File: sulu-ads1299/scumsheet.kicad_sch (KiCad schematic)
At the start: 23 parts

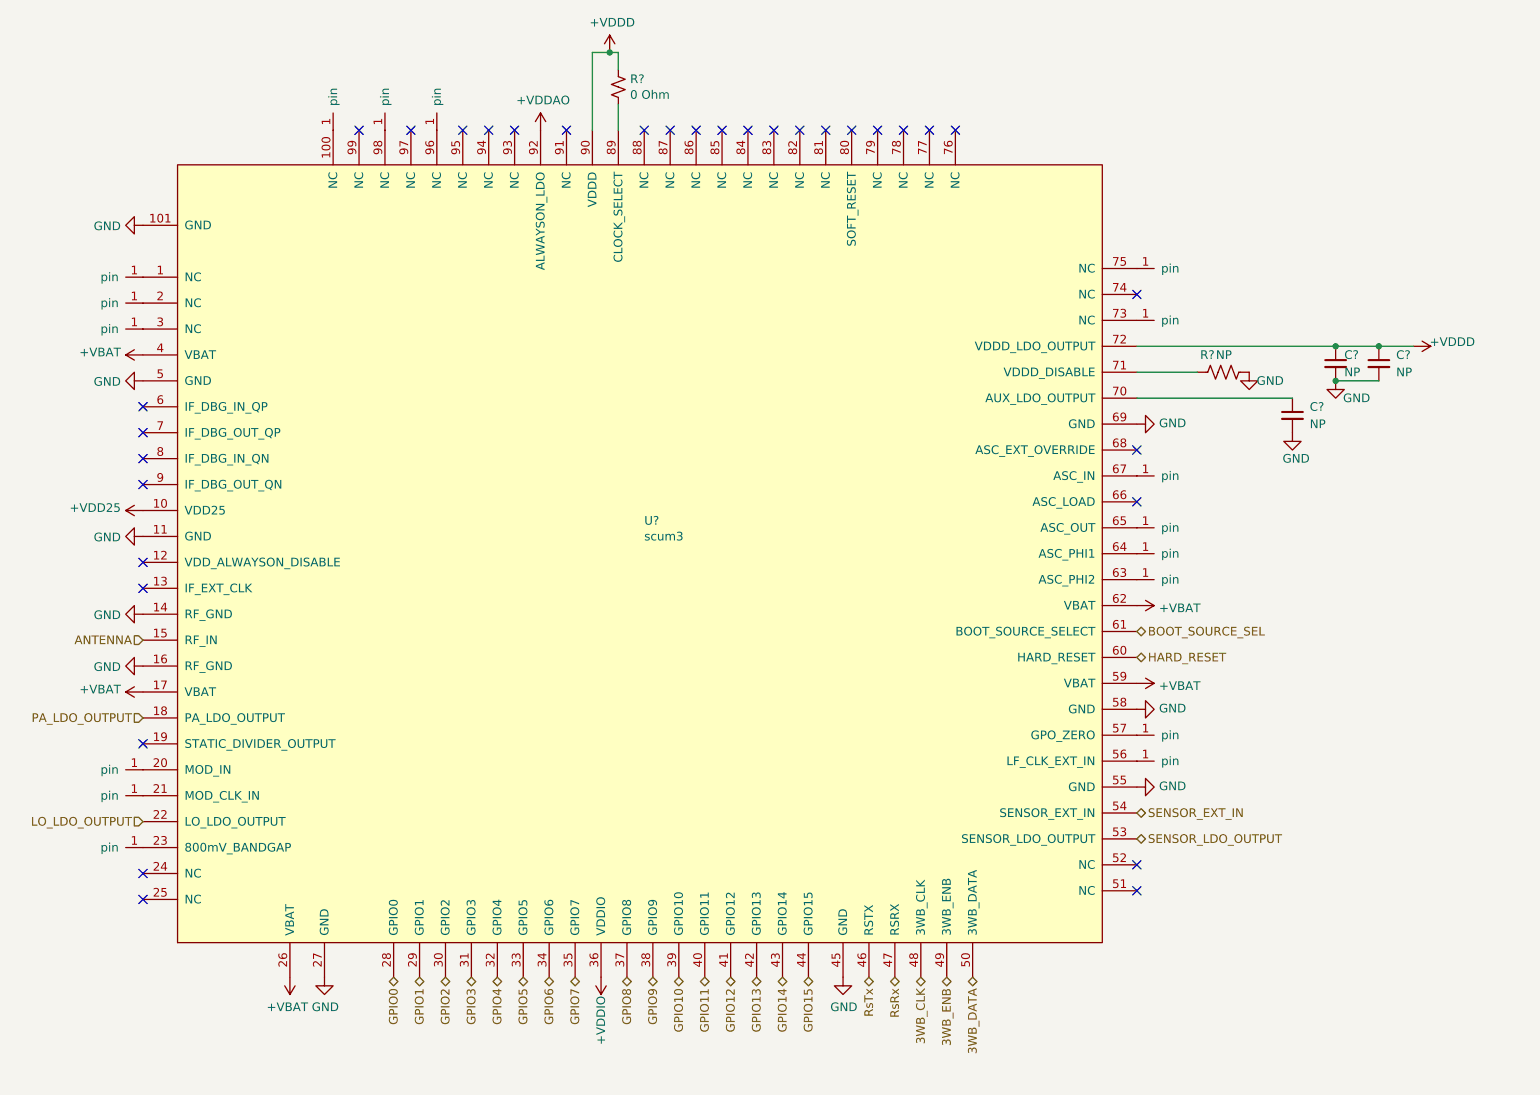
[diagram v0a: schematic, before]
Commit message: Sulu-ads1299 schematic largely completed
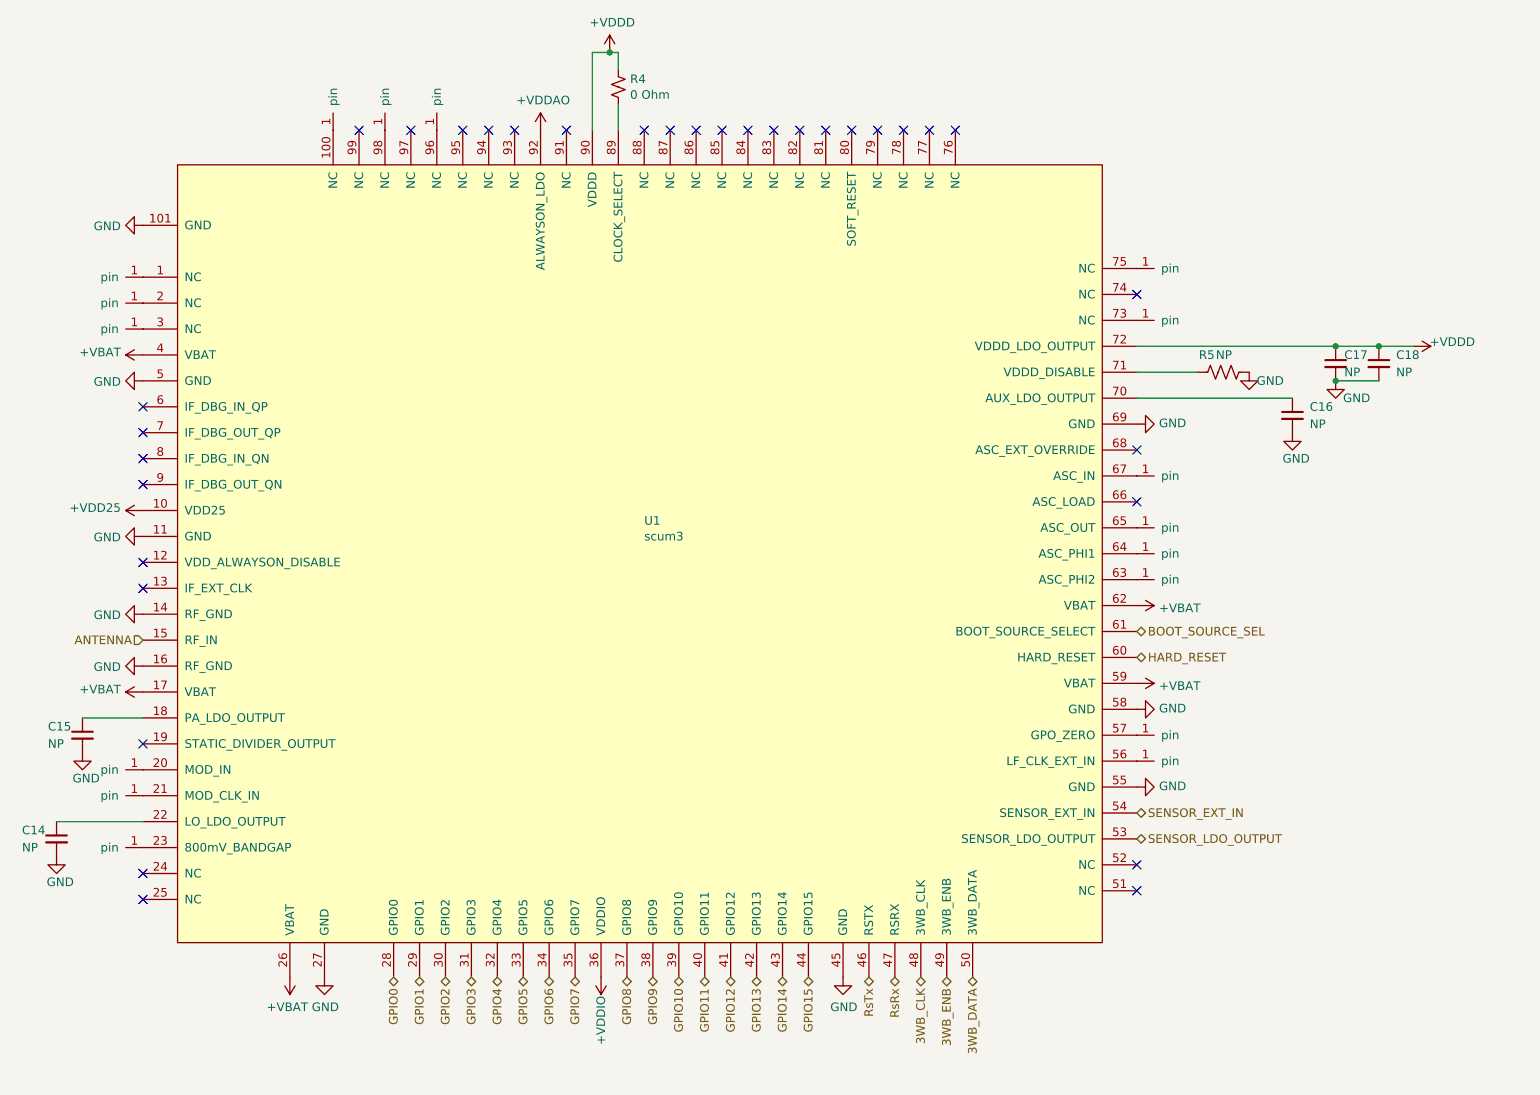
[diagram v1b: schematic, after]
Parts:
- added C14, C15: NP, symbol Device:C_Small
- gave numbers to parts that had none: 23
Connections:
- net GND: now also C14.2, C15.2
- net LO_LDO_OUTPUT: no longer names the net of U1.22 (LO_LDO_OUTPUT)
- net LO_LDO_OUTPUT: now also C14.1
- net PA_LDO_OUTPUT: no longer names the net of U1.18 (PA_LDO_OUTPUT)
- net PA_LDO_OUTPUT: now also C15.1

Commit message: Sulu-ads1299 started layout & imported shared footprints
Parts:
- C14, C15, C16, C17, C18: footprint (none) -> Capacitor_SMD:C_0402_1005Metric
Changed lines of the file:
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@@
       (effects (font (size 1.27 1.27)) (justify left))
     )
-    (property "Footprint" "" (id 2) (at 245.11 63.5 0)
+    (property "Footprint" "Capacitor_SMD:C_0402_1005Metric" (id 2) (at 245.11 63.5 0)
       (effects (font (size 1.27 1.27)) hide)
     )
@@
       (effects (font (size 1.27 1.27)) (justify left))
     )
-    (property "Footprint" "" (id 2) (at 238.76 63.5 0)
+    (property "Footprint" "Capacitor_SMD:C_0402_1005Metric" (id 2) (at 238.76 63.5 0)
       (effects (font (size 1.27 1.27)) hide)
     )
@@
       (effects (font (size 1.27 1.27)) (justify left))
     )
-    (property "Footprint" "" (id 2) (at 50.8 133.35 0)
+    (property "Footprint" "Capacitor_SMD:C_0402_1005Metric" (id 2) (at 50.8 133.35 0)
       (effects (font (size 1.27 1.27)) hide)
     )
@@
       (effects (font (size 1.27 1.27)) (justify left))
     )
-    (property "Footprint" "" (id 2) (at 232.41 71.12 0)
+    (property "Footprint" "Capacitor_SMD:C_0402_1005Metric" (id 2) (at 232.41 71.12 0)
       (effects (font (size 1.27 1.27)) hide)
     )
@@
       (effects (font (size 1.27 1.27)) (justify left))
     )
-    (property "Footprint" "" (id 2) (at 54.61 118.11 0)
-      (effects (font (size 1.27 1.27)) hide)
-    )
+    (property "Footprint" "Capacitor_SMD:C_0402_1005Metric" (id 2) (at 54.61 118.11 0)
+      (effects (font (size 1.27 1.27)) hide)
+    )

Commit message: Sulu-ads1299 finalized floorplan, began routing, updated schematic
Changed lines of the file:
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@@
       (effects (font (size 1.27 1.27)) (justify left))
     )
-    (property "Value" "NP" (id 1) (at 223.52 62.23 90)
+    (property "Value" "NP" (id 1) (at 220.98 66.04 90)
       (effects (font (size 1.27 1.27)) (justify left))
     )

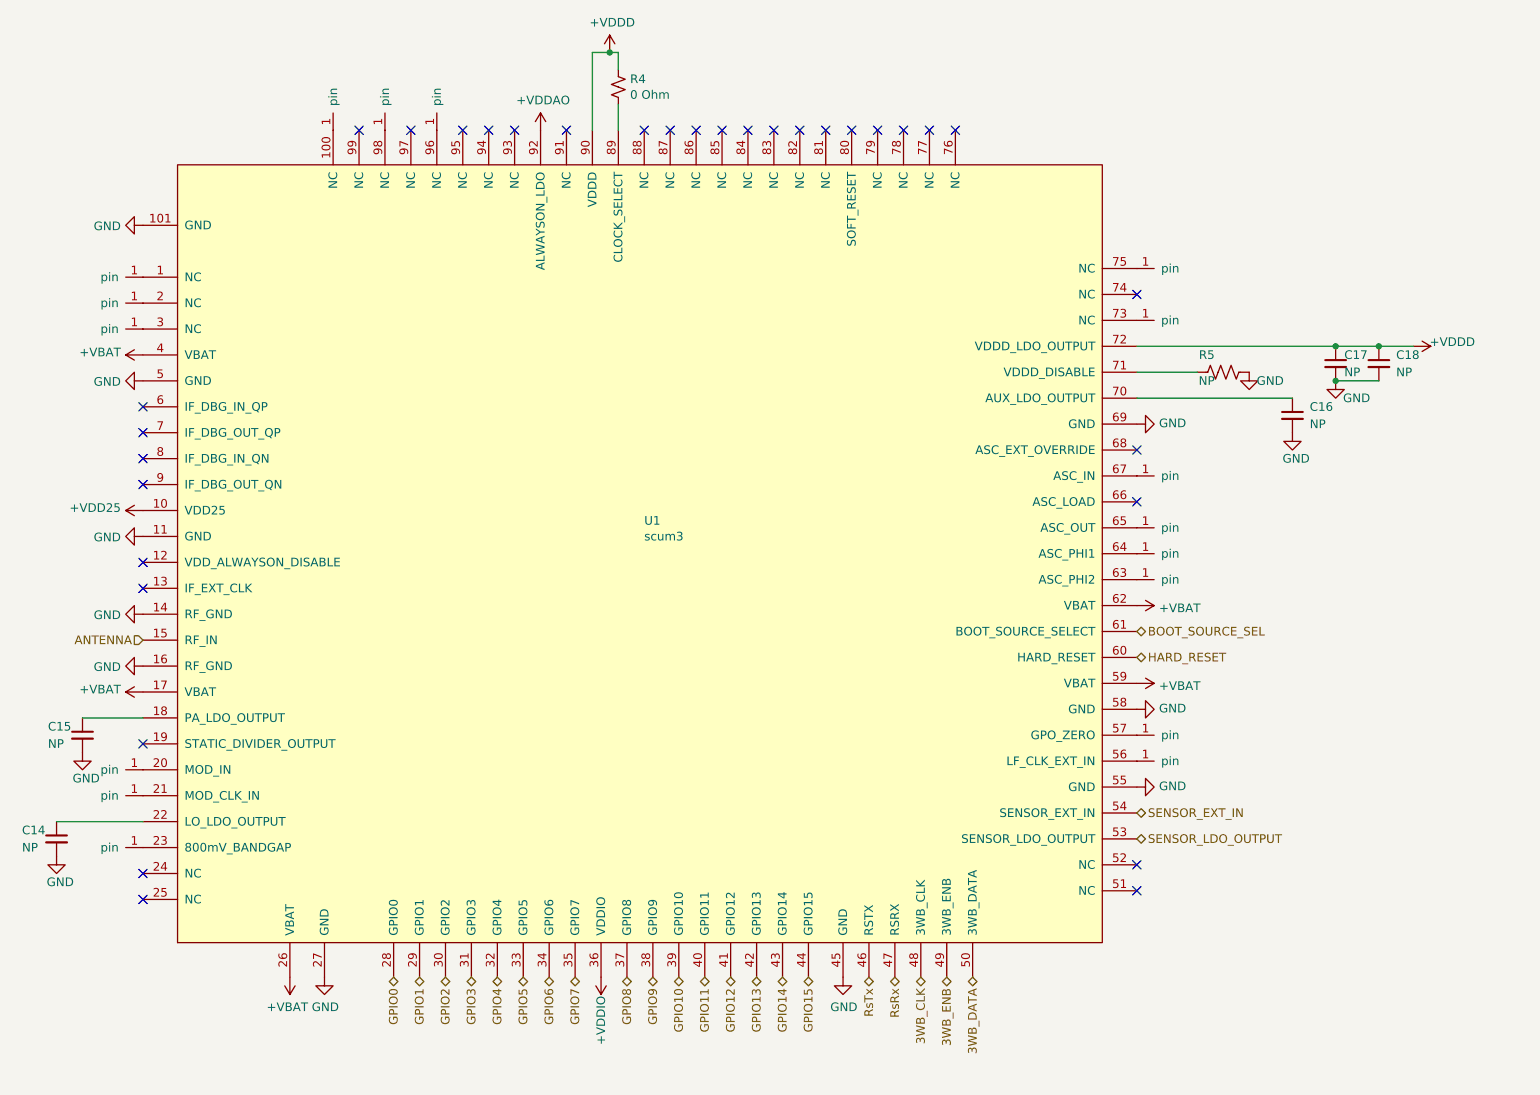
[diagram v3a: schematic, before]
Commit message: Sulu-ads1299, completed place & route
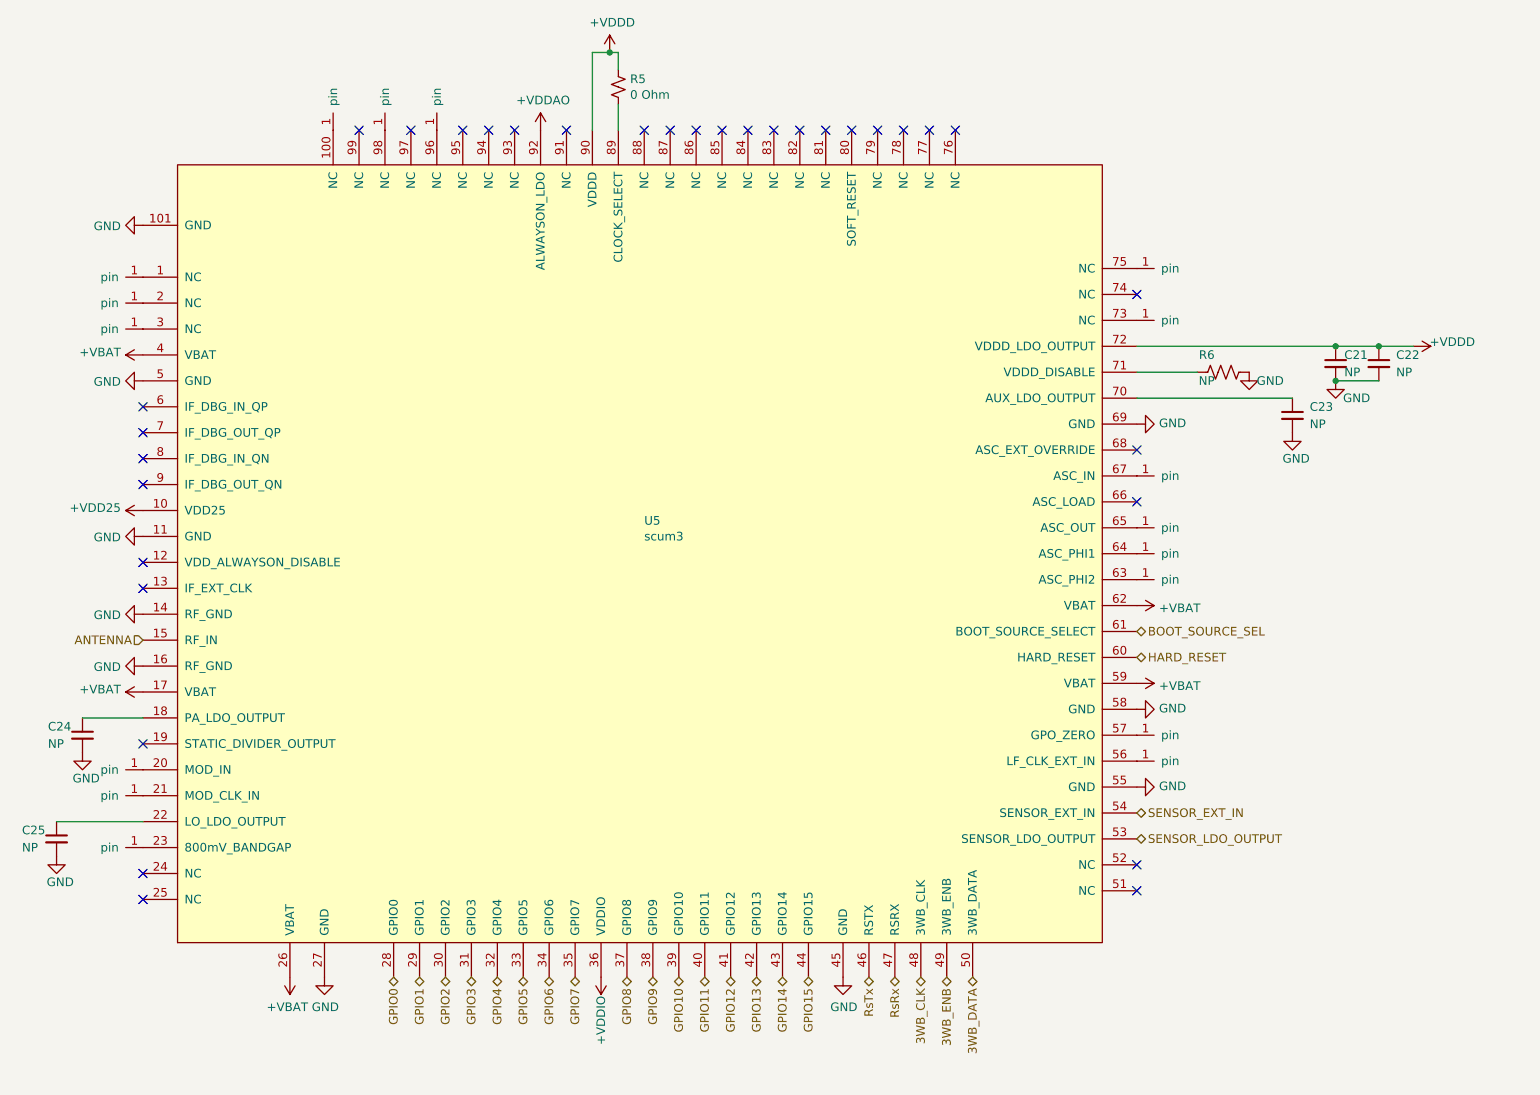
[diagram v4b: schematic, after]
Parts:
- renumbered C17 to C21, C18 to C22, C16 to C23, C15 to C24, C14 to C25, J14 to J10, J15 to J11, J16 to J12, J7 to J13, J8 to J14, J17 to J15, J9 to J16, J18 to J17, J19 to J18, J20 to J19, J21 to J20, J22 to J21, J23 to J22, J10 to J23, J11 to J24, J12 to J25, J13 to J9, R4 to R5, R5 to R6, U1 to U5

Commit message: Upated schematic and layout.
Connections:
- net +VBAT: no longer U5.17 (VBAT), U5.26 (VBAT), U5.59 (VBAT)
- no-connect marks 33 -> 36
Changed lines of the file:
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@@
   )
   (no_connect (at 102.87 29.21))
+  (no_connect (at 85.09 153.67))
   (no_connect (at 125.73 29.21))
   (no_connect (at 209.55 76.2))
@@
   (no_connect (at 179.07 29.21))
   (no_connect (at 95.25 29.21))
+  (no_connect (at 209.55 110.49))
   (no_connect (at 63.5 142.24))
   (no_connect (at 110.49 29.21))
@@
   (no_connect (at 63.5 77.47))
   (no_connect (at 160.02 29.21))
+  (no_connect (at 63.5 111.76))
   (no_connect (at 163.83 29.21))
   (no_connect (at 63.5 92.71))
@@
     )
     (property "Datasheet" "" (id 3) (at 209.55 95.25 0)
-      (effects (font (size 1.27 1.27)) hide)
-    )
-    (pin "1")
-  )
-  (symbol (lib_id "draft1library:+VBAT") (at 85.09 153.67 180) (unit 1)
-    (in_bom yes) (on_board yes)
-    (property "Reference" "#PWR0105" (id 0) (at 85.09 149.86 0)
-      (effects (font (size 1.27 1.27)) hide)
-    )
-    (property "Value" "+VBAT" (id 1) (at 84.709 158.0642 0))
-    (property "Footprint" "" (id 2) (at 85.09 153.67 0)
-      (effects (font (size 1.27 1.27)) hide)
-    )
-    (property "Datasheet" "" (id 3) (at 85.09 153.67 0)
-      (effects (font (size 1.27 1.27)) hide)
-    )
-    (pin "1")
-  )
-  (symbol (lib_id "draft1library:+VBAT") (at 209.55 110.49 270) (unit 1)
-    (in_bom yes) (on_board yes)
-    (property "Reference" "#PWR099" (id 0) (at 205.74 110.49 0)
-      (effects (font (size 1.27 1.27)) hide)
-    )
-    (property "Value" "+VBAT" (id 1) (at 212.8012 110.871 90)
-      (effects (font (size 1.27 1.27)) (justify left))
-    )
-    (property "Footprint" "" (id 2) (at 209.55 110.49 0)
-      (effects (font (size 1.27 1.27)) hide)
-    )
-    (property "Datasheet" "" (id 3) (at 209.55 110.49 0)
       (effects (font (size 1.27 1.27)) hide)
     )
@@
       (effects (font (size 1.27 1.27)) hide)
     )
-    (pin "1")
-  )
-  (symbol (lib_id "draft1library:+VBAT") (at 63.5 111.76 90) (unit 1)
-    (in_bom yes) (on_board yes)
-    (property "Reference" "#PWR0100" (id 0) (at 67.31 111.76 0)
-      (effects (font (size 1.27 1.27)) hide)
-    )
-    (property "Value" "+VBAT" (id 1) (at 60.2488 111.379 90)
-      (effects (font (size 1.27 1.27)) (justify left))
-    )
-    (property "Footprint" "" (id 2) (at 63.5 111.76 0)
-      (effects (font (size 1.27 1.27)) hide)
-    )
-    (property "Datasheet" "" (id 3) (at 63.5 111.76 0)
-      (effects (font (size 1.27 1.27)) hide)
-    )
